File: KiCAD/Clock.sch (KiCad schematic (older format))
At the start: 25 parts, among them SW301 PULSE_CLK, U301 74HCT32N, U302 74LS04, U303 LM555, U304 LM555, U305 74HCT08N

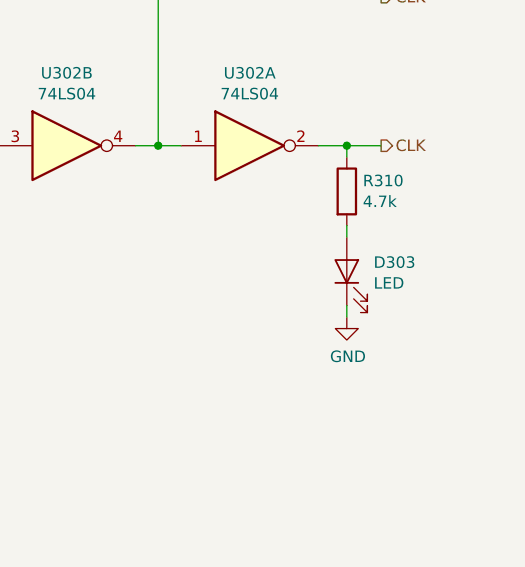
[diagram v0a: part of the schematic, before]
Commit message: Moved SP out of register module into SP module; changed RS0 assert signal alias from RS0 to RSH; moved uCode and program code to different subdirs of Programming/ .
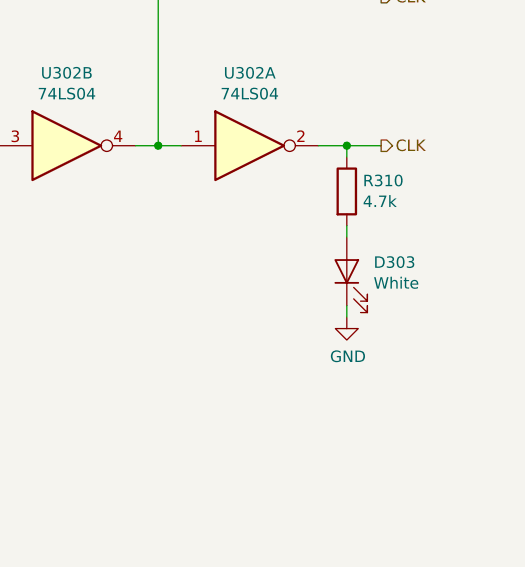
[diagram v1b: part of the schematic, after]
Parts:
- D303: value LED -> White
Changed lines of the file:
@@
 P 14725 3775
 F 0 "D303" V 14764 3658 50  0000 R CNN
-F 1 "LED" V 14673 3658 50  0000 R CNN
+F 1 "White" V 14673 3658 50  0000 R CNN
 F 2 "" H 14725 3775 50  0001 C CNN
 F 3 "~" H 14725 3775 50  0001 C CNN

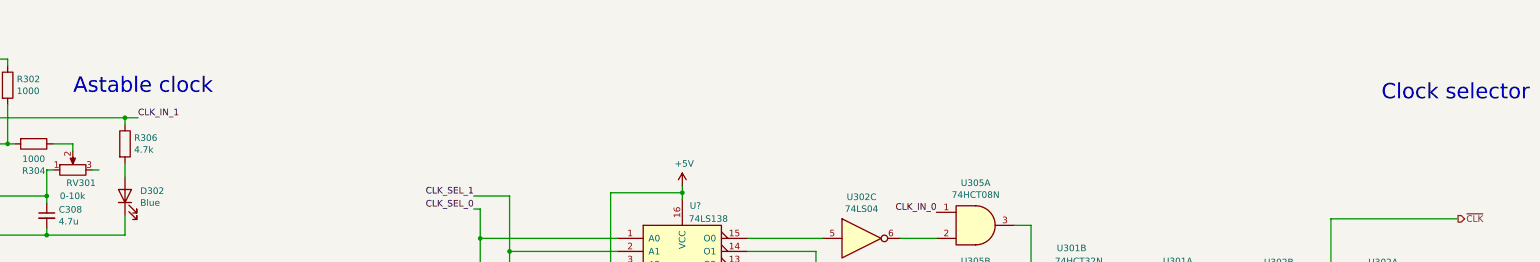
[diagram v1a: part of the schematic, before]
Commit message: Finish OSR for multiline string prints
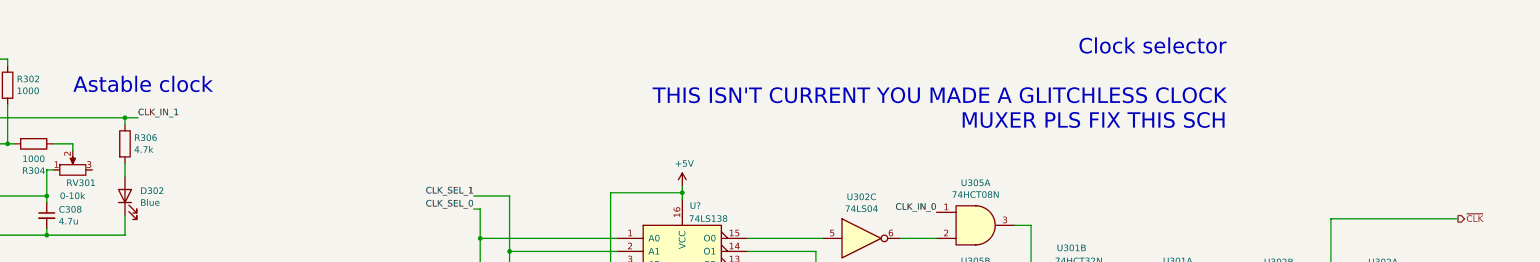
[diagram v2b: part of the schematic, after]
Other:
- note added: "Clock selector\n\nTHIS ISN'T CURRENT YOU MADE A GLITCHLESS CLOCK\nMUXER PLS FIX THIS SCH"
- note removed: "Clock selector"
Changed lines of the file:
@@
 Wire Wire Line
 	3650 2400 3650 2500
-Wire Wire Line
-	4450 2200 4400 2200
 $Comp
 L Breadboard_CPU-rescue:LED-Device D302
@@
 Text Notes 3900 3525 0    118  ~ 0
 Debounced button
-Text Notes 15425 1675 2    118  ~ 0
-Clock selector
+Text Notes 13100 1900 2    118  ~ 0
+Clock selector\n\nTHIS ISN'T CURRENT YOU MADE A GLITCHLESS CLOCK\nMUXER PLS FIX THIS SCH
 $Comp
 L Breadboard_CPU-rescue:74LS08-74xx U?
